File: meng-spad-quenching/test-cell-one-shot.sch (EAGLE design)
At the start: 41 parts, among them IC1 NC7SV74K8X, IC2 LTC1711, IC3 DS1100LU-20+, M1 BSS806N, X1 CONN_3V3_PWR, X2 CONN_ONE_SHOT_OUT, X3 CONN_TRIG_IN, X4 CONN_ONE_SHOT_OUT_DLY

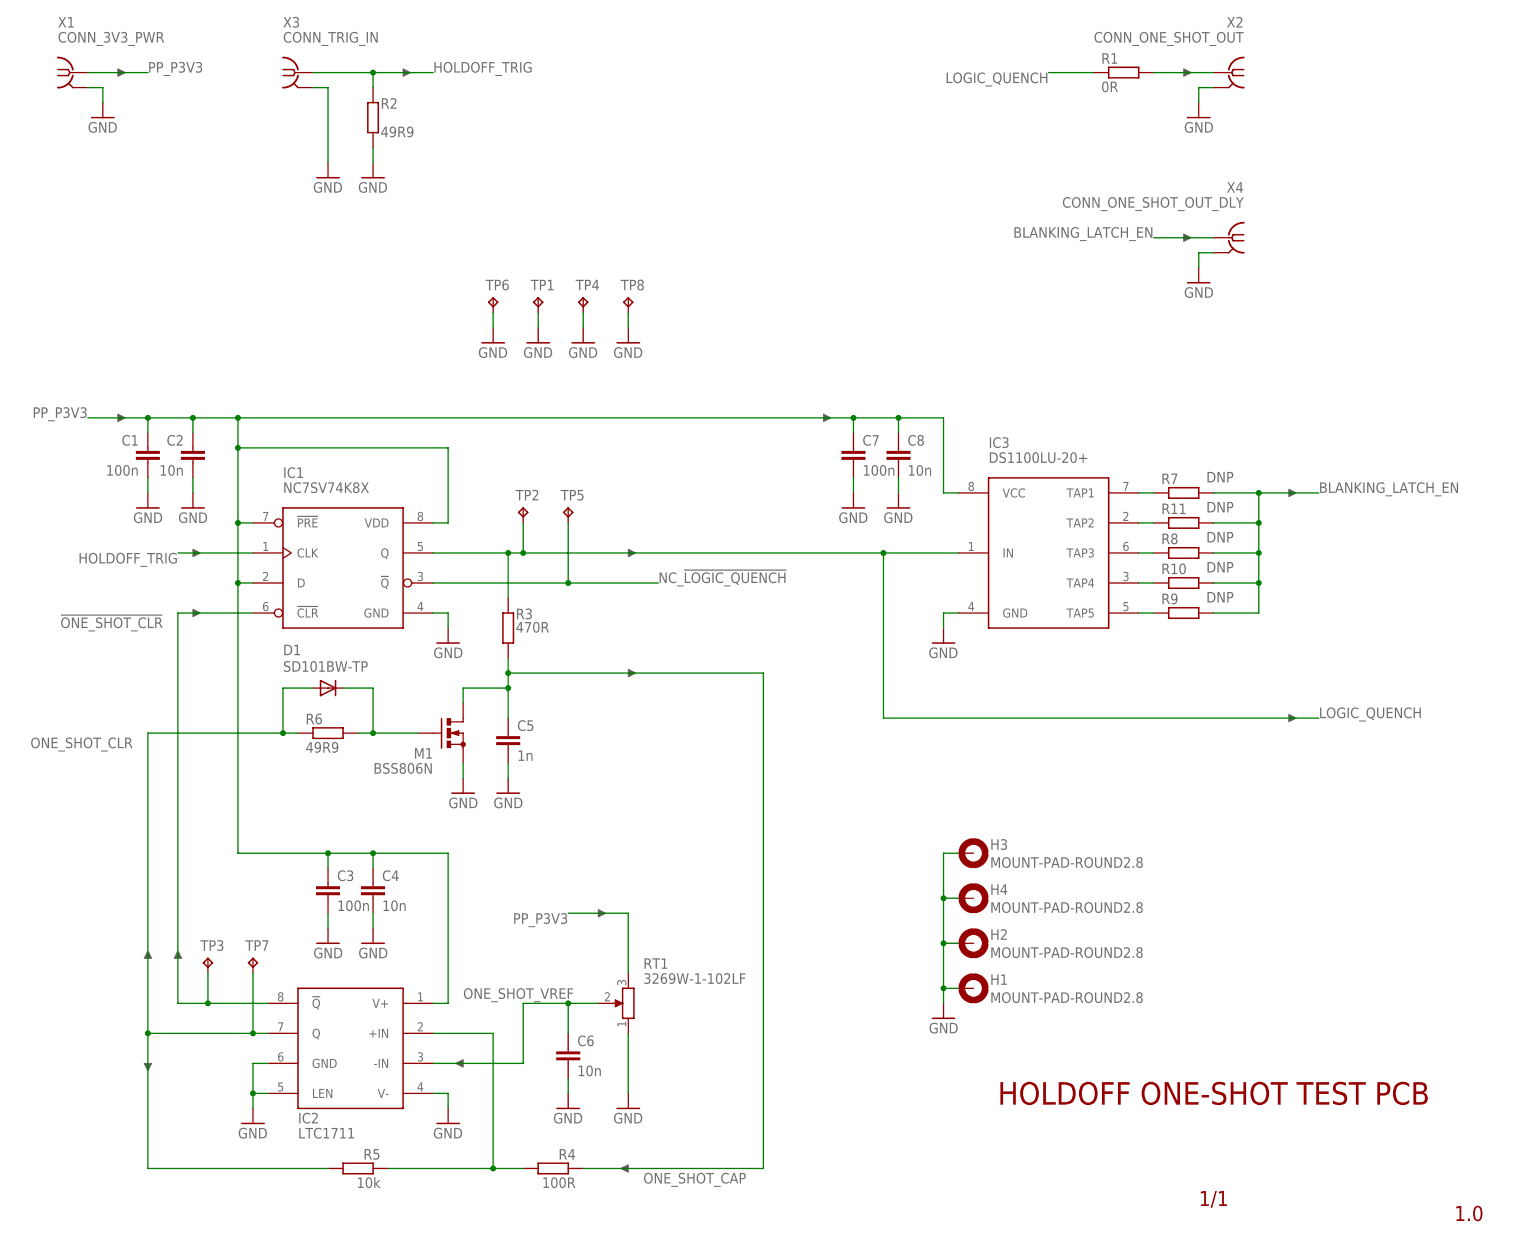
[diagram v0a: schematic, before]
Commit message: Added EXT vref conn, finalized gerbers
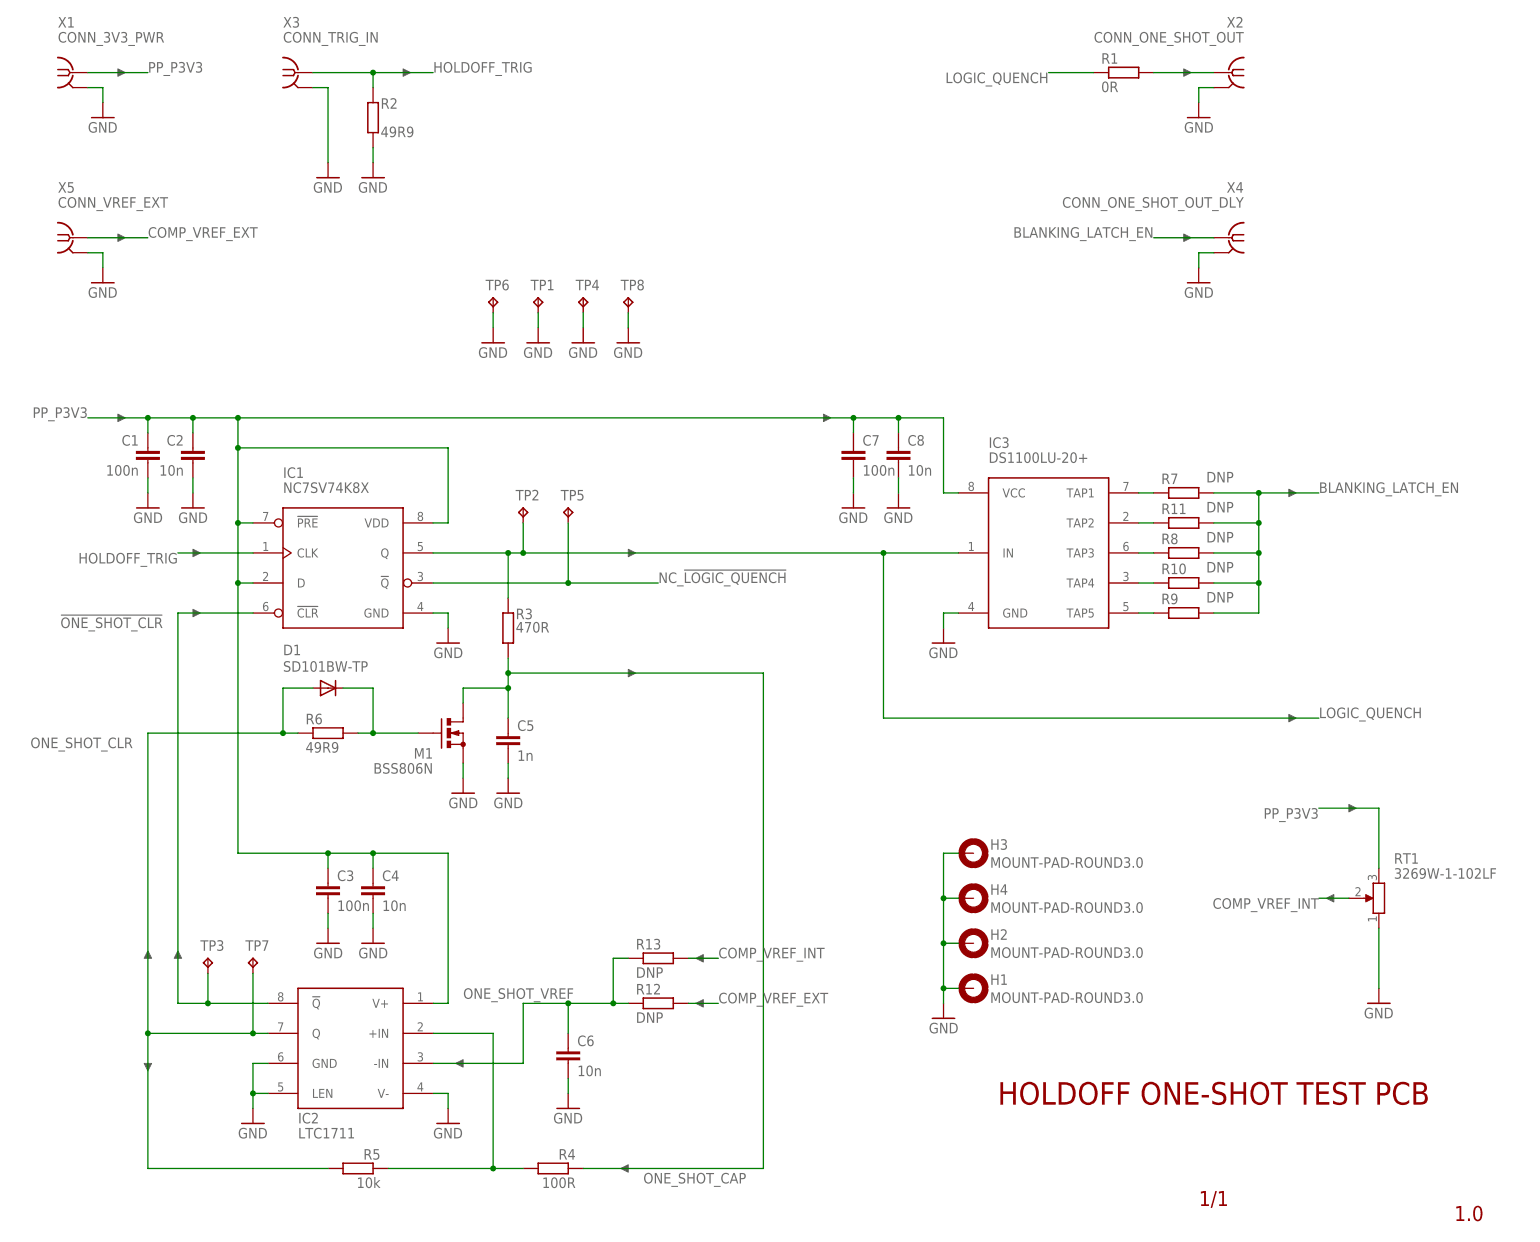
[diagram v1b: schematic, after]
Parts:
- added R12, R13: DNP, rcl:R-EU_R0402
- added X5: CONN_VREF_EXT, con-coax:SMA-142-0711-871/876
- H1, H2, H3, H4: value MOUNT-PAD-ROUND2.8 -> MOUNT-PAD-ROUND3.0; device holes:MOUNT-PAD-ROUND2.8 -> holes:MOUNT-PAD-ROUND3.0
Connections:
- new net COMP_VREF_EXT: R12.1, X5G1.1
- new net COMP_VREF_INT: R13.1, RT1.2
- net GND: now also X5G1.GND
- net ONE_SHOT_VREF: now also R12.2, R13.2; no longer RT1.2
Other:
- moved on the sheet: RT1
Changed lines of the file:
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@@
 <part name="R1" library="rcl" deviceset="R-EU_" device="R0402" value="0R"/>
 <part name="DNP3" library="meng" deviceset="ARROW_1DIR" device=""/>
-<part name="H3" library="holes" deviceset="MOUNT-PAD-ROUND" device="2.8"/>
-<part name="H4" library="holes" deviceset="MOUNT-PAD-ROUND" device="2.8"/>
-<part name="H2" library="holes" deviceset="MOUNT-PAD-ROUND" device="2.8"/>
-<part name="H1" library="holes" deviceset="MOUNT-PAD-ROUND" device="2.8"/>
+<part name="H3" library="holes" deviceset="MOUNT-PAD-ROUND" device="3.0"/>
+<part name="H4" library="holes" deviceset="MOUNT-PAD-ROUND" device="3.0"/>
+<part name="H2" library="holes" deviceset="MOUNT-PAD-ROUND" device="3.0"/>
+<part name="H1" library="holes" deviceset="MOUNT-PAD-ROUND" device="3.0"/>
 <part name="GND12" library="supply1" deviceset="GND" device=""/>
 <part name="TP2" library="testpad" deviceset="TP" device="TP10R"/>
@@
 <part name="GND15" library="supply1" deviceset="GND" device=""/>
 <part name="GND16" library="supply1" deviceset="GND" device=""/>
+<part name="X5" library="con-coax" deviceset="SMA-" device="142-0711-871/876" value="CONN_VREF_EXT"/>
+<part name="GND17" library="supply1" deviceset="GND" device=""/>
+<part name="DNP7" library="meng" deviceset="ARROW_1DIR" device=""/>
+<part name="DNP8" library="meng" deviceset="ARROW_1DIR" device=""/>
+<part name="R12" library="rcl" deviceset="R-EU_" device="R0402" value="DNP"/>
+<part name="R13" library="rcl" deviceset="R-EU_" device="R0402" value="DNP"/>
+<part name="DNP9" library="meng" deviceset="ARROW_1DIR" device=""/>
+<part name="DNP10" library="meng" deviceset="ARROW_1DIR" device=""/>
 </parts>
 <sheets>
@@
 <text x="228.6" y="185.42" size="1.778" layer="98" rot="MR0">To scope</text>
 <text x="228.6" y="157.48" size="1.778" layer="98" rot="MR0">To scope</text>
-<text x="127" y="40.64" size="1.778" layer="98">1k</text>
+<text x="254" y="58.42" size="1.778" layer="98">1k</text>
+<text x="27.94" y="157.48" size="1.778" layer="98">From power supply</text>
 </plain>
 <instances>
@@
 <attribute name="VALUE" x="111.76" y="22.86" size="1.778" layer="96"/>
 </instance>
-<instance part="RT1" gate="G$1" x="124.46" y="43.18" smashed="yes" rot="R180">
-<attribute name="NAME" x="127" y="50.8" size="1.778" layer="95" rot="MR180"/>
-<attribute name="VALUE" x="127" y="48.26" size="1.778" layer="96" rot="MR180"/>
-</instance>
-<instance part="GND10" gate="1" x="124.46" y="25.4" smashed="yes">
-<attribute name="VALUE" x="121.92" y="22.86" size="1.778" layer="96"/>
-</instance>
-<instance part="DNP5" gate="G$1" x="119.38" y="58.42" smashed="yes"/>
+<instance part="RT1" gate="G$1" x="251.46" y="60.96" smashed="yes" rot="R180">
+<attribute name="NAME" x="254" y="68.58" size="1.778" layer="95" rot="MR180"/>
+<attribute name="VALUE" x="254" y="66.04" size="1.778" layer="96" rot="MR180"/>
+</instance>
+<instance part="GND10" gate="1" x="251.46" y="43.18" smashed="yes">
+<attribute name="VALUE" x="248.92" y="40.64" size="1.778" layer="96"/>
+</instance>
+<instance part="DNP5" gate="G$1" x="246.38" y="76.2" smashed="yes"/>
 <instance part="R2" gate="G$1" x="81.28" y="193.04" smashed="yes" rot="R270">
 <attribute name="NAME" x="82.55" y="194.5386" size="1.778" layer="95"/>
@@
 <attribute name="VALUE" x="121.92" y="152.4" size="1.778" layer="96"/>
 </instance>
+<instance part="X5" gate="G1" x="30.48" y="172.72" smashed="yes">
+<attribute name="VALUE" x="27.94" y="177.8" size="1.778" layer="96"/>
+<attribute name="NAME" x="27.94" y="180.34" size="1.778" layer="95"/>
+</instance>
+<instance part="GND17" gate="1" x="35.56" y="165.1" smashed="yes">
+<attribute name="VALUE" x="33.02" y="162.56" size="1.778" layer="96"/>
+</instance>
+<instance part="DNP7" gate="G$1" x="38.1" y="172.72" smashed="yes" rot="MR180"/>
+<instance part="DNP8" gate="G$1" x="243.84" y="60.96" smashed="yes" rot="R180"/>
+<instance part="R12" gate="G$1" x="129.54" y="43.18" smashed="yes" rot="R180">
+<attribute name="NAME" x="125.73" y="44.6786" size="1.778" layer="95"/>
+<attribute name="VALUE" x="125.73" y="39.878" size="1.778" layer="96"/>
+</instance>
+<instance part="R13" gate="G$1" x="129.54" y="50.8" smashed="yes" rot="R180">
+<attribute name="NAME" x="125.73" y="52.2986" size="1.778" layer="95"/>
+<attribute name="VALUE" x="125.73" y="47.498" size="1.778" layer="96"/>
+</instance>
+<instance part="DNP9" gate="G$1" x="137.16" y="43.18" smashed="yes" rot="R180"/>
+<instance part="DNP10" gate="G$1" x="137.16" y="50.8" smashed="yes" rot="R180"/>
 </instances>
 <busses>
@@
 <pinref part="GND10" gate="1" pin="GND"/>
 <pinref part="RT1" gate="G$1" pin="1"/>
-<wire x1="124.46" y1="27.94" x2="124.46" y2="38.1" width="0.1524" layer="91"/>
+<wire x1="251.46" y1="45.72" x2="251.46" y2="55.88" width="0.1524" layer="91"/>
 </segment>
 <segment>
@@
 <pinref part="TP8" gate="G$1" pin="TP"/>
 <wire x1="124.46" y1="157.48" x2="124.46" y2="160.02" width="0.1524" layer="91"/>
+</segment>
+<segment>
+<pinref part="X5" gate="G1" pin="GND"/>
+<wire x1="33.02" y1="170.18" x2="35.56" y2="170.18" width="0.1524" layer="91"/>
+<wire x1="35.56" y1="170.18" x2="35.56" y2="167.64" width="0.1524" layer="91"/>
+<pinref part="GND17" gate="1" pin="GND"/>
 </segment>
 </net>
@@
 </segment>
 <segment>
-<wire x1="124.46" y1="58.42" x2="114.3" y2="58.42" width="0.1524" layer="91"/>
-<label x="114.3" y="58.42" size="1.778" layer="95" rot="R180"/>
+<wire x1="251.46" y1="76.2" x2="241.3" y2="76.2" width="0.1524" layer="91"/>
+<label x="241.3" y="76.2" size="1.778" layer="95" rot="R180"/>
 <pinref part="RT1" gate="G$1" pin="3"/>
-<wire x1="124.46" y1="48.26" x2="124.46" y2="58.42" width="0.1524" layer="91"/>
+<wire x1="251.46" y1="66.04" x2="251.46" y2="76.2" width="0.1524" layer="91"/>
 </segment>
 </net>
@@
 <label x="96.52" y="45.72" size="1.778" layer="95" rot="MR180"/>
 <pinref part="C6" gate="G$1" pin="1"/>
-<wire x1="114.3" y1="43.18" x2="119.38" y2="43.18" width="0.1524" layer="91"/>
 <wire x1="114.3" y1="38.1" x2="114.3" y2="43.18" width="0.1524" layer="91"/>
+<pinref part="R12" gate="G$1" pin="2"/>
+<wire x1="114.3" y1="43.18" x2="121.92" y2="43.18" width="0.1524" layer="91"/>
+<pinref part="R13" gate="G$1" pin="2"/>
+<wire x1="121.92" y1="43.18" x2="124.46" y2="43.18" width="0.1524" layer="91"/>
+<wire x1="124.46" y1="50.8" x2="121.92" y2="50.8" width="0.1524" layer="91"/>
+<wire x1="121.92" y1="50.8" x2="121.92" y2="43.18" width="0.1524" layer="91"/>
+<junction x="121.92" y="43.18"/>
 <junction x="114.3" y="43.18"/>
-<pinref part="RT1" gate="G$1" pin="2"/>
 </segment>
 </net>
@@
 </segment>
 </net>
+<net name="COMP_VREF_EXT" class="0">
+<segment>
+<pinref part="X5" gate="G1" pin="1"/>
+<wire x1="33.02" y1="172.72" x2="43.18" y2="172.72" width="0.1524" layer="91"/>
+<label x="43.18" y="172.72" size="1.778" layer="95"/>
+</segment>
+<segment>
+<pinref part="R12" gate="G$1" pin="1"/>
+<wire x1="134.62" y1="43.18" x2="139.7" y2="43.18" width="0.1524" layer="91"/>
+<label x="139.7" y="43.18" size="1.778" layer="95"/>
+</segment>
+</net>
+<net name="COMP_VREF_INT" class="0">
+<segment>
+<pinref part="RT1" gate="G$1" pin="2"/>
+<wire x1="246.38" y1="60.96" x2="241.3" y2="60.96" width="0.1524" layer="91"/>
+<label x="241.3" y="60.96" size="1.778" layer="95" rot="R180"/>
+</segment>
+<segment>
+<pinref part="R13" gate="G$1" pin="1"/>
+<wire x1="134.62" y1="50.8" x2="139.7" y2="50.8" width="0.1524" layer="91"/>
+<label x="139.7" y="50.8" size="1.778" layer="95"/>
+</segment>
+</net>
